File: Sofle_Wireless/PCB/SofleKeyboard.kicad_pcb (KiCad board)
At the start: 2 copper layers, 144 x 115.7 mm, 121 parts, among them J1 Conn_01x05, SW1 SW1, SW10 SW10, SW11 SW11, SW12 SW12, SW13 SW13, SW14 SW14, SW15 SW15, SW16 SW16, SW17 SW17, SW18 SW18, SW19 SW19, SW2 SW2, SW20 SW20, SW21 SW21, SW22 SW22, SW23 SW23, SW24 SW24, SW25 SW19, SW26 SW26, SW27 SW27, SW28 SW28, SW29 SW29, SW3 SW3, SW30 SW30, SW4 SW4, SW5 SW5, SW6 SW6, SW7 SW7, SW8 SW8, SW9 SW9, U1 NICE!NANO

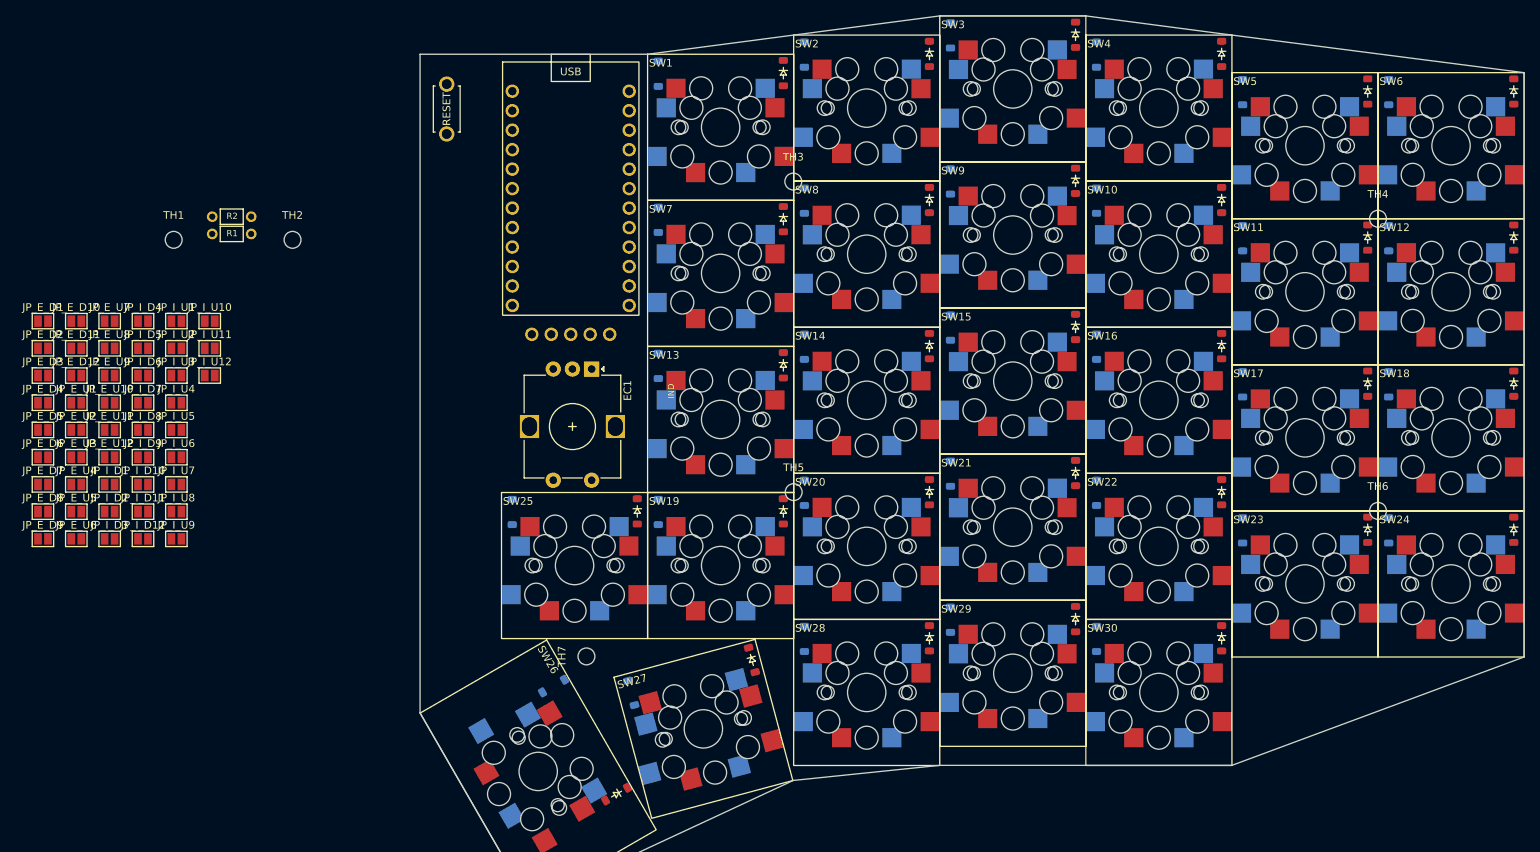
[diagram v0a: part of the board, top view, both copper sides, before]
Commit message: Work on Footprints, PCB and schematic
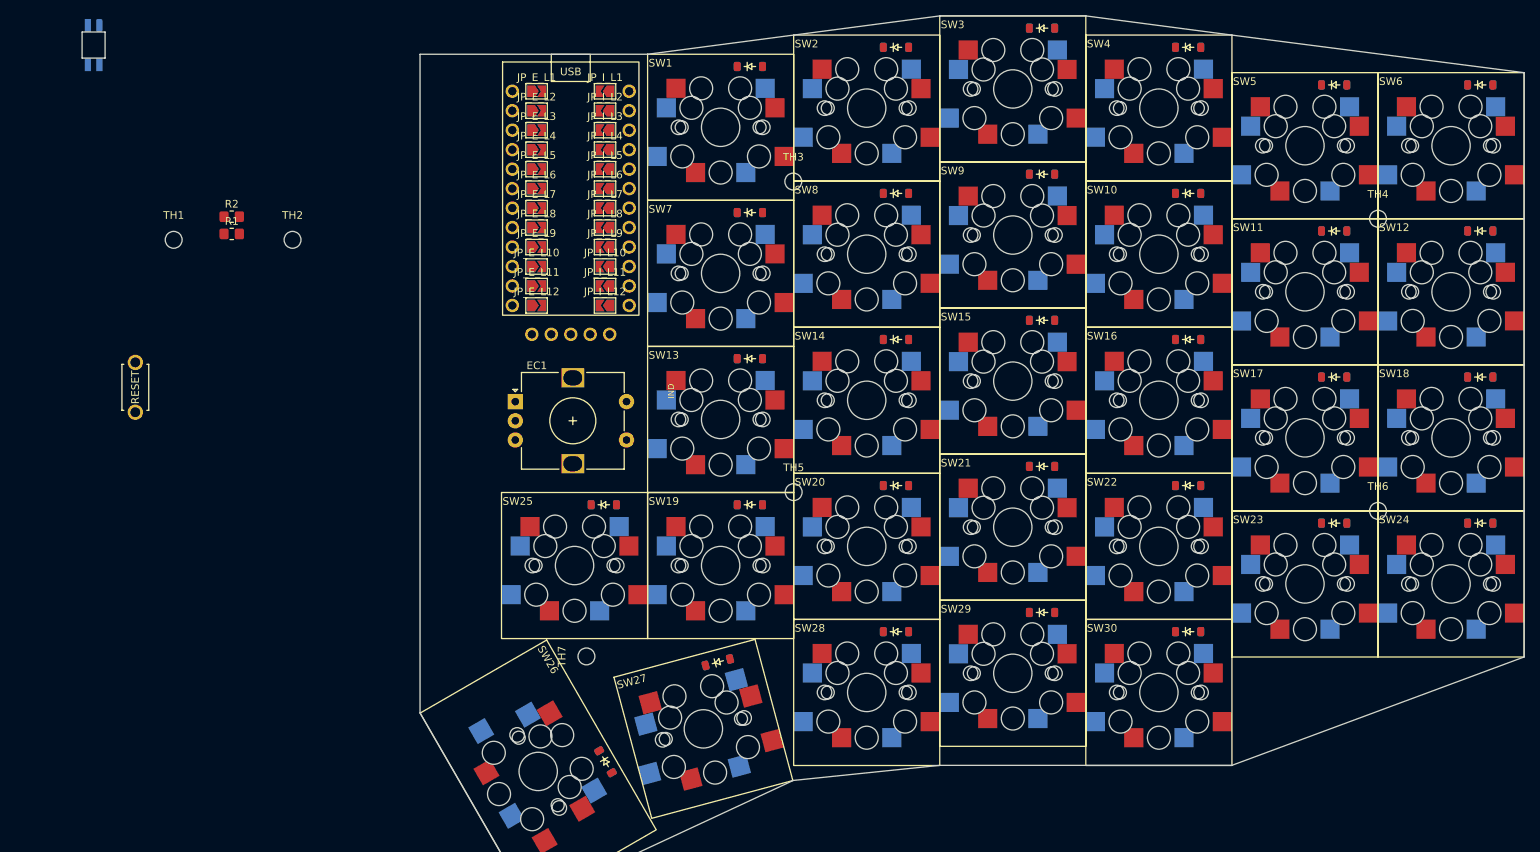
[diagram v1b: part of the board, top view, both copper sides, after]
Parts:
- removed JP_E_D1, JP_E_D10, JP_E_D11, JP_E_D12, JP_E_D2, JP_E_D3, JP_E_D4, JP_E_D5, JP_E_D6, JP_E_D7, JP_E_D8, JP_E_D9, JP_E_U1, JP_E_U10, JP_E_U11, JP_E_U12, JP_E_U2, JP_E_U3, JP_E_U4, JP_E_U5, JP_E_U6, JP_E_U7, JP_E_U8, JP_E_U9, JP_I_D1, JP_I_D10, JP_I_D11, JP_I_D12, JP_I_D2, JP_I_D3, JP_I_D4, JP_I_D5, JP_I_D6, JP_I_D7, JP_I_D8, JP_I_D9, JP_I_U1, JP_I_U10, JP_I_U11, JP_I_U12, JP_I_U2, JP_I_U3, JP_I_U4, JP_I_U5, JP_I_U6, JP_I_U7, JP_I_U8, JP_I_U9: Jumper_NO_Small, Jumper:SolderJumper-2_P1.3mm_Open_Pad1.0x1.5mm
- added D31: LED_SK6812MINI, ScottoKeebs_Components:LED_SK6812MINI, F.Cu at (38.7, 39.3)
- added JP_E_L1: Jumper_NO_Small, Mechanical_Switches:SolderJumper-2_P1.3mm_Open_TrianglePad1.0x1.5mm_E, F.Cu at (96.5, 45.3)
- added JP_E_L10: Jumper_NO_Small, Mechanical_Switches:SolderJumper-2_P1.3mm_Open_TrianglePad1.0x1.5mm_E, F.Cu at (96.5, 68.2)
- added JP_E_L11: Jumper_NO_Small, Mechanical_Switches:SolderJumper-2_P1.3mm_Open_TrianglePad1.0x1.5mm_E, F.Cu at (96.5, 70.7)
- added JP_E_L12: Jumper_NO_Small, Mechanical_Switches:SolderJumper-2_P1.3mm_Open_TrianglePad1.0x1.5mm_E, F.Cu at (96.5, 73.2)
- added JP_E_L2: Jumper_NO_Small, Mechanical_Switches:SolderJumper-2_P1.3mm_Open_TrianglePad1.0x1.5mm_E, F.Cu at (96.5, 47.8)
- added JP_E_L3: Jumper_NO_Small, Mechanical_Switches:SolderJumper-2_P1.3mm_Open_TrianglePad1.0x1.5mm_E, F.Cu at (96.5, 50.4)
- added JP_E_L4: Jumper_NO_Small, Mechanical_Switches:SolderJumper-2_P1.3mm_Open_TrianglePad1.0x1.5mm_E, F.Cu at (96.5, 52.9)
- added JP_E_L5: Jumper_NO_Small, Mechanical_Switches:SolderJumper-2_P1.3mm_Open_TrianglePad1.0x1.5mm_E, F.Cu at (96.5, 55.5)
- added JP_E_L6: Jumper_NO_Small, Mechanical_Switches:SolderJumper-2_P1.3mm_Open_TrianglePad1.0x1.5mm_E, F.Cu at (96.5, 58.0)
- added JP_E_L7: Jumper_NO_Small, Mechanical_Switches:SolderJumper-2_P1.3mm_Open_TrianglePad1.0x1.5mm_E, F.Cu at (96.5, 60.5)
- added JP_E_L8: Jumper_NO_Small, Mechanical_Switches:SolderJumper-2_P1.3mm_Open_TrianglePad1.0x1.5mm_E, F.Cu at (96.5, 63.1)
- added JP_E_L9: Jumper_NO_Small, Mechanical_Switches:SolderJumper-2_P1.3mm_Open_TrianglePad1.0x1.5mm_E, F.Cu at (96.5, 65.6)
- added JP_E_R1: Jumper_NO_Small, Mechanical_Switches:SolderJumper-2_P1.3mm_Open_TrianglePad1.0x1.5mm_E_Reverse, F.Cu at (96.5, 45.3)
- added JP_E_R10: Jumper_NO_Small, Mechanical_Switches:SolderJumper-2_P1.3mm_Open_TrianglePad1.0x1.5mm_E_Reverse, F.Cu at (96.5, 68.2)
- added JP_E_R11: Jumper_NO_Small, Mechanical_Switches:SolderJumper-2_P1.3mm_Open_TrianglePad1.0x1.5mm_E_Reverse, F.Cu at (96.5, 70.7)
- added JP_E_R12: Jumper_NO_Small, Mechanical_Switches:SolderJumper-2_P1.3mm_Open_TrianglePad1.0x1.5mm_E_Reverse, F.Cu at (96.5, 73.2)
- added JP_E_R2: Jumper_NO_Small, Mechanical_Switches:SolderJumper-2_P1.3mm_Open_TrianglePad1.0x1.5mm_E_Reverse, F.Cu at (96.5, 47.8)
- added JP_E_R3: Jumper_NO_Small, Mechanical_Switches:SolderJumper-2_P1.3mm_Open_TrianglePad1.0x1.5mm_E_Reverse, F.Cu at (96.5, 50.4)
- added JP_E_R4: Jumper_NO_Small, Mechanical_Switches:SolderJumper-2_P1.3mm_Open_TrianglePad1.0x1.5mm_E_Reverse, F.Cu at (96.5, 52.9)
- added JP_E_R5: Jumper_NO_Small, Mechanical_Switches:SolderJumper-2_P1.3mm_Open_TrianglePad1.0x1.5mm_E_Reverse, F.Cu at (96.5, 55.5)
- added JP_E_R6: Jumper_NO_Small, Mechanical_Switches:SolderJumper-2_P1.3mm_Open_TrianglePad1.0x1.5mm_E_Reverse, F.Cu at (96.5, 58.0)
- added JP_E_R7: Jumper_NO_Small, Mechanical_Switches:SolderJumper-2_P1.3mm_Open_TrianglePad1.0x1.5mm_E_Reverse, F.Cu at (96.5, 60.5)
- added JP_E_R8: Jumper_NO_Small, Mechanical_Switches:SolderJumper-2_P1.3mm_Open_TrianglePad1.0x1.5mm_E_Reverse, F.Cu at (96.5, 63.1)
- added JP_E_R9: Jumper_NO_Small, Mechanical_Switches:SolderJumper-2_P1.3mm_Open_TrianglePad1.0x1.5mm_E_Reverse, F.Cu at (96.5, 65.6)
- added JP_I_L1: Jumper_NO_Small, Mechanical_Switches:SolderJumper-2_P1.3mm_Open_TrianglePad1.0x1.5mm_I, F.Cu at (105.4, 45.3)
- added JP_I_L10: Jumper_NO_Small, Mechanical_Switches:SolderJumper-2_P1.3mm_Open_TrianglePad1.0x1.5mm_I, F.Cu at (105.4, 68.2)
- added JP_I_L11: Jumper_NO_Small, Mechanical_Switches:SolderJumper-2_P1.3mm_Open_TrianglePad1.0x1.5mm_I, F.Cu at (105.4, 70.7)
- added JP_I_L12: Jumper_NO_Small, Mechanical_Switches:SolderJumper-2_P1.3mm_Open_TrianglePad1.0x1.5mm_I, F.Cu at (105.4, 73.2)
- added JP_I_L2: Jumper_NO_Small, Mechanical_Switches:SolderJumper-2_P1.3mm_Open_TrianglePad1.0x1.5mm_I, F.Cu at (105.4, 47.8)
- added JP_I_L3: Jumper_NO_Small, Mechanical_Switches:SolderJumper-2_P1.3mm_Open_TrianglePad1.0x1.5mm_I, F.Cu at (105.4, 50.4)
- added JP_I_L4: Jumper_NO_Small, Mechanical_Switches:SolderJumper-2_P1.3mm_Open_TrianglePad1.0x1.5mm_I, F.Cu at (105.4, 52.9)
- added JP_I_L5: Jumper_NO_Small, Mechanical_Switches:SolderJumper-2_P1.3mm_Open_TrianglePad1.0x1.5mm_I, F.Cu at (105.4, 55.5)
- added JP_I_L6: Jumper_NO_Small, Mechanical_Switches:SolderJumper-2_P1.3mm_Open_TrianglePad1.0x1.5mm_I, F.Cu at (105.4, 58.0)
- added JP_I_L7: Jumper_NO_Small, Mechanical_Switches:SolderJumper-2_P1.3mm_Open_TrianglePad1.0x1.5mm_I, F.Cu at (105.4, 60.5)
- added JP_I_L8: Jumper_NO_Small, Mechanical_Switches:SolderJumper-2_P1.3mm_Open_TrianglePad1.0x1.5mm_I, F.Cu at (105.4, 63.1)
- added JP_I_L9: Jumper_NO_Small, Mechanical_Switches:SolderJumper-2_P1.3mm_Open_TrianglePad1.0x1.5mm_I, F.Cu at (105.4, 65.6)
- added JP_I_R1: Jumper_NO_Small, Mechanical_Switches:SolderJumper-2_P1.3mm_Open_TrianglePad1.0x1.5mm_I_Reverse, F.Cu at (105.4, 45.3)
- added JP_I_R10: Jumper_NO_Small, Mechanical_Switches:SolderJumper-2_P1.3mm_Open_TrianglePad1.0x1.5mm_I_Reverse, F.Cu at (105.4, 68.2)
- added JP_I_R11: Jumper_NO_Small, Mechanical_Switches:SolderJumper-2_P1.3mm_Open_TrianglePad1.0x1.5mm_I_Reverse, F.Cu at (105.4, 70.7)
- added JP_I_R12: Jumper_NO_Small, Mechanical_Switches:SolderJumper-2_P1.3mm_Open_TrianglePad1.0x1.5mm_I_Reverse, F.Cu at (105.4, 73.2)
- added JP_I_R2: Jumper_NO_Small, Mechanical_Switches:SolderJumper-2_P1.3mm_Open_TrianglePad1.0x1.5mm_I_Reverse, F.Cu at (105.4, 47.8)
- added JP_I_R3: Jumper_NO_Small, Mechanical_Switches:SolderJumper-2_P1.3mm_Open_TrianglePad1.0x1.5mm_I_Reverse, F.Cu at (105.4, 50.4)
- added JP_I_R4: Jumper_NO_Small, Mechanical_Switches:SolderJumper-2_P1.3mm_Open_TrianglePad1.0x1.5mm_I_Reverse, F.Cu at (105.4, 52.9)
- added JP_I_R5: Jumper_NO_Small, Mechanical_Switches:SolderJumper-2_P1.3mm_Open_TrianglePad1.0x1.5mm_I_Reverse, F.Cu at (105.4, 55.5)
- added JP_I_R6: Jumper_NO_Small, Mechanical_Switches:SolderJumper-2_P1.3mm_Open_TrianglePad1.0x1.5mm_I_Reverse, F.Cu at (105.4, 58.0)
- added JP_I_R7: Jumper_NO_Small, Mechanical_Switches:SolderJumper-2_P1.3mm_Open_TrianglePad1.0x1.5mm_I_Reverse, F.Cu at (105.4, 60.5)
- added JP_I_R8: Jumper_NO_Small, Mechanical_Switches:SolderJumper-2_P1.3mm_Open_TrianglePad1.0x1.5mm_I_Reverse, F.Cu at (105.4, 63.1)
- added JP_I_R9: Jumper_NO_Small, Mechanical_Switches:SolderJumper-2_P1.3mm_Open_TrianglePad1.0x1.5mm_I_Reverse, F.Cu at (105.4, 65.6)
- EC1: footprint Rotary_Encoder:RotaryEncoder_Alps_EC12E-Switch_Vertical_H20mm -> Mechanical_Switches:RotaryEncoder_Alps_EC12E-Switch_Vertical_H20mm
- R1, R2: footprint kbd:R -> Resistor_SMD:R_0805_2012Metric_Pad1.20x1.40mm_HandSolder
- moved RSW1 54.5 mm to (44.2, 83.9)
- moved EC1 10.8 mm to (93.7, 85.8), turned to 0 degrees
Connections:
- J1 pad 1: unconnected-(J1-Pin_1-Pad1) -> SDA
- J1 pad 2: unconnected-(J1-Pin_2-Pad2) -> SCL
- J1 pad 3: unconnected-(J1-Pin_3-Pad3) -> VCC
- J1 pad 4: unconnected-(J1-Pin_4-Pad4) -> GND
- J1 pad 5: unconnected-(J1-Pin_5-Pad5) -> CS

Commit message: Work on traces
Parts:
- added D32: LED_SK6812MINI, RGB_LED:SK6812_Mini-E_DualSide, F.Cu at (86.1, 83.5)
- added D33: LED_SK6812MINI, RGB_LED:SK6812_Mini-E_DualSide, F.Cu at (86.1, 87.0)
- added D34: LED_SK6812MINI, RGB_LED:SK6812_Mini-E_DualSide, F.Cu at (86.1, 91.7)
- added D35: LED_SK6812MINI, RGB_LED:SK6812_Mini-E_DualSide, F.Cu at (86.1, 96.4)
- added D36: LED_SK6812MINI, RGB_LED:SK6812_Mini-E_DualSide, F.Cu at (86.1, 101.1)
- added D37: LED_SK6812MINI, RGB_LED:SK6812_Mini-E_DualSide, F.Cu at (86.1, 105.8)
- added D38: LED_SK6812MINI, RGB_LED:SK6812_Mini-E_DualSide, F.Cu at (86.1, 110.6)
- added D39: LED_SK6812MINI, RGB_LED:SK6812_Mini-E_DualSide, F.Cu at (86.1, 115.3)
- added D40: LED_SK6812MINI, RGB_LED:SK6812_Mini-E_DualSide, F.Cu at (86.1, 120.0)
- added D41: LED_SK6812MINI, RGB_LED:SK6812_Mini-E_DualSide, F.Cu at (101.4, 88.2)
- added JP_ENC_LA1: Jumper_NO_Small, Mechanical_Switches:SolderJumper-2_P1.3mm_Open_TrianglePad1.0x1.5mm_E, F.Cu at (59.2, 90.8)
- added JP_ENC_LB1: Jumper_NO_Small, Mechanical_Switches:SolderJumper-2_P1.3mm_Open_TrianglePad1.0x1.5mm_E, F.Cu at (59.2, 93.9)
- added JP_ENC_RA1: Jumper_NO_Small, Mechanical_Switches:SolderJumper-2_P1.3mm_Open_TrianglePad1.0x1.5mm_E_Reverse, F.Cu at (94.0, 80.1)
- added JP_ENC_RB1: Jumper_NO_Small, Mechanical_Switches:SolderJumper-2_P1.3mm_Open_TrianglePad1.0x1.5mm_E_Reverse, F.Cu at (91.9, 80.1)
- added JP_LCD_L1: Jumper_NO_Small, Mechanical_Switches:SolderJumper-2_P1.3mm_Open_TrianglePad1.0x1.5mm_E, F.Cu at (63.1, 93.9)
- added JP_LCD_L2: Jumper_NO_Small, Mechanical_Switches:SolderJumper-2_P1.3mm_Open_TrianglePad1.0x1.5mm_E, F.Cu at (63.1, 97.0)
- added JP_LCD_L4: Jumper_NO_Small, Mechanical_Switches:SolderJumper-2_P1.3mm_Open_TrianglePad1.0x1.5mm_E, F.Cu at (67.0, 90.8)
- added JP_LCD_L5: Jumper_NO_Small, Mechanical_Switches:SolderJumper-2_P1.3mm_Open_TrianglePad1.0x1.5mm_E, F.Cu at (67.0, 93.9)
- added JP_LCD_R1: Jumper_NO_Small, Mechanical_Switches:SolderJumper-2_P1.3mm_Open_TrianglePad1.0x1.5mm_E_Reverse, F.Cu at (89.3, 70.2)
- added JP_LCD_R2: Jumper_NO_Small, Mechanical_Switches:SolderJumper-2_P1.3mm_Open_TrianglePad1.0x1.5mm_E_Reverse, F.Cu at (89.3, 67.7)
- added JP_LCD_R4: Jumper_NO_Small, Mechanical_Switches:SolderJumper-2_P1.3mm_Open_TrianglePad1.0x1.5mm_E_Reverse, F.Cu at (89.4, 65.1)
- added JP_LCD_R5: Jumper_NO_Small, Mechanical_Switches:SolderJumper-2_P1.3mm_Open_TrianglePad1.0x1.5mm_E_Reverse, F.Cu at (89.4, 62.6)
- D31: footprint ScottoKeebs_Components:LED_SK6812MINI -> RGB_LED:SK6812_Mini-E_DualSide
- R1, R2: footprint Resistor_SMD:R_0805_2012Metric_Pad1.20x1.40mm_HandSolder -> Mechanical_Switches:R_0805_2012Metric_Pad1.20x1.40mm_HandSolder_dualside
- moved D31 62.3 mm to (86.1, 79.8), turned to 0 degrees
- moved RSW1 53.9 mm to (86.3, 50.4), turned to 180 degrees
- moved R2 14.1 mm to (68.0, 53.2), turned to -90 degrees
- moved R1 14.1 mm to (65.8, 53.2), turned to -90 degrees
- moved J1 0.48 mm to (101.3, 77.3)
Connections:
- net SW25A renamed col5
- net SW25B renamed Net-(D25-A)
- D31 pad 1: unconnected-(D31-DOUT-Pad1) -> VCC
- D31 pad 2: GND -> Net-(D31-DOUT)
- D31 pad 3: LED -> GND
- D31 pad 4: VCC -> LED
- EC1 pad A: ENCA -> Net-(EC1-PadA)
- EC1 pad B: ENCB -> Net-(EC1-PadB)
- J1 pad 1: SDA -> Net-(J1-Pin_1)
- J1 pad 2: SCL -> Net-(J1-Pin_2)
- J1 pad 4: GND -> Net-(J1-Pin_4)
- J1 pad 5: CS -> Net-(J1-Pin_5)
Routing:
- net col0: track 0.00 -> 286.0 mm, vias 0 -> 22
- net col1: track 0.00 -> 276.4 mm, vias 0 -> 19
- net col2: track 0.00 -> 254.7 mm, vias 0 -> 17
- net col3: track 0.00 -> 241.0 mm, vias 0 -> 15
- net col4: track 0.00 -> 210.3 mm, vias 0 -> 13
- net row3: track 0.00 -> 172.6 mm, vias 0 -> 7
- net col5: track 0.00 -> 170.7 mm, vias 0 -> 11
- net row0: track 0.00 -> 157.5 mm, vias 0 -> 7
- net row4: track 0.00 -> 156.6 mm, vias 0 -> 7
- net row2: track 0.00 -> 153.5 mm, vias 0 -> 7
- net row1: track 0.00 -> 142.8 mm, vias 0 -> 7
- net Net-(D25-A): track 0.00 -> 31.0 mm, vias 0 -> 1
- net Net-(D26-A): track 0.00 -> 23.2 mm, vias 0 -> 1
- net Net-(D23-A): track 0.00 -> 23.1 mm, vias 0 -> 1
- net Net-(D27-A): track 0.00 -> 22.9 mm, vias 0 -> 1
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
